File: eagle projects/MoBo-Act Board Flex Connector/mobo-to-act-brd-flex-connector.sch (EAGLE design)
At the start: 2 parts

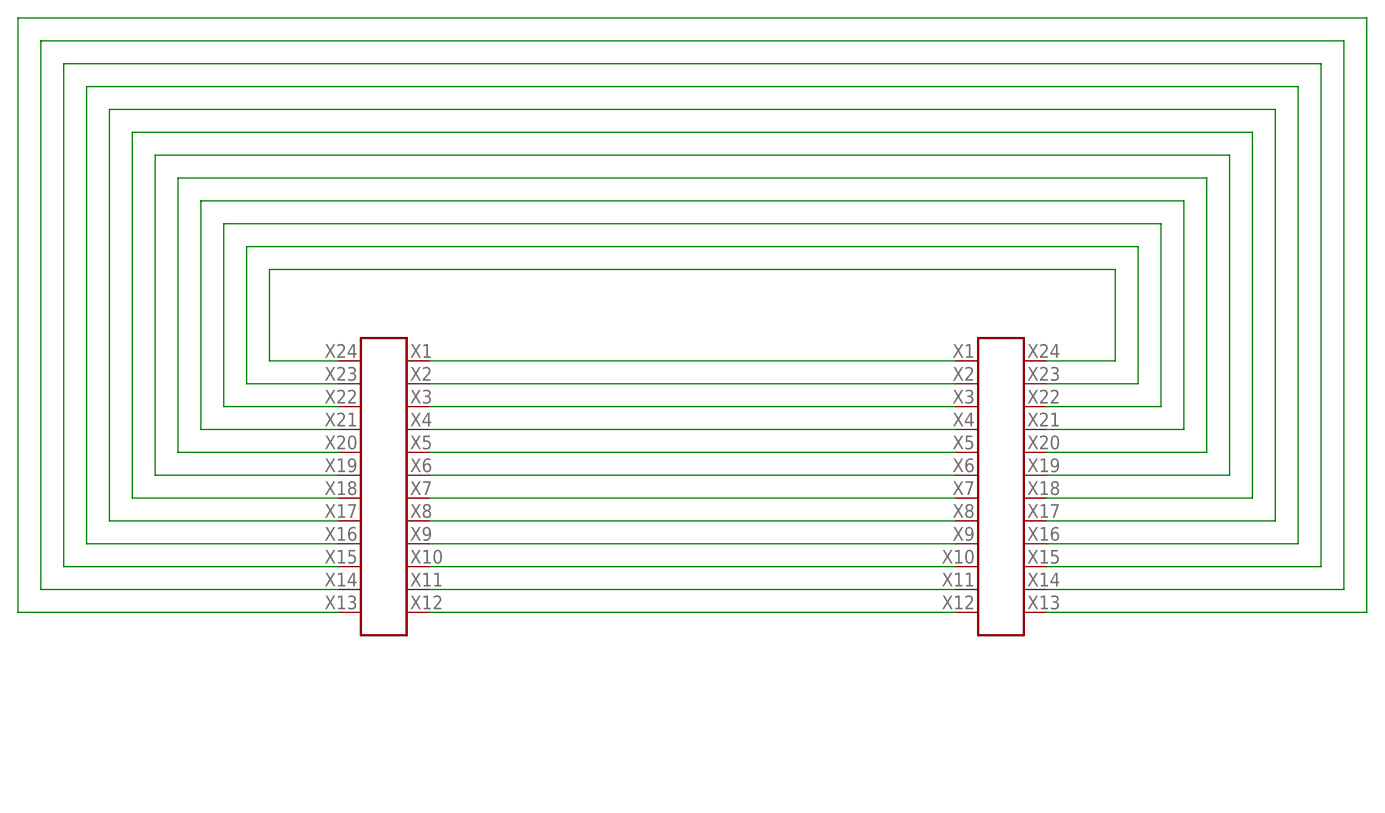
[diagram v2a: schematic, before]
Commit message: Fixed Connector Boards
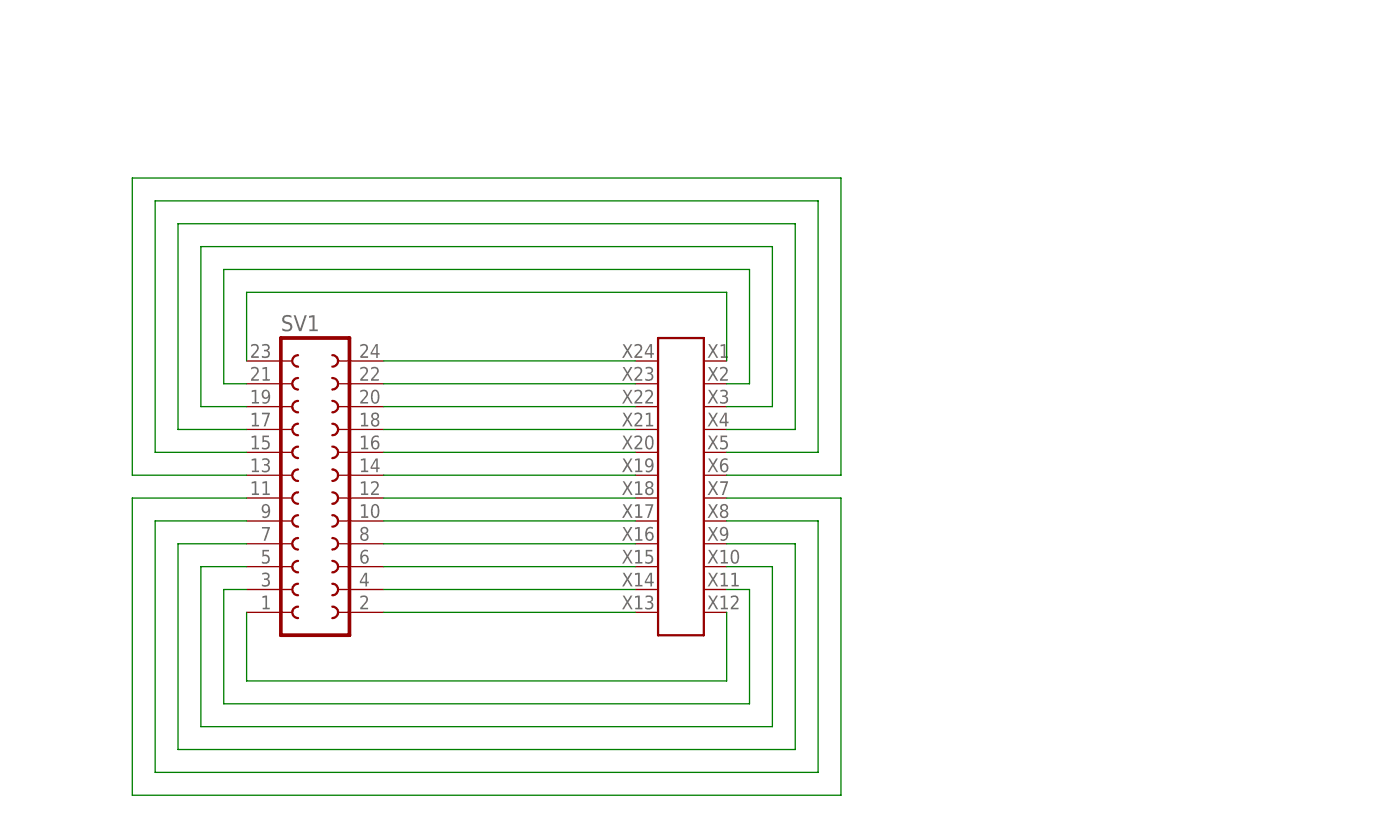
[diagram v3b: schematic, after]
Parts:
- removed U$1: 12X2_SMD_2.54MM_HEADER, SMD_headers:12X2_SMD_2.54MM_HEADER
- added SV1: (no value), con-lsta:FE12-2
- U$2: value 12X2_MIRRORED_SMD_2.54MM_HEADER -> 12X2_SMD_2.54MM_HEADER; device SMD_headers:12X2_MIRRORED_SMD_2.54MM_HEADER -> SMD_headers:12X2_SMD_2.54MM_HEADER
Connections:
- net N$1: now also SV1.1, U$2.P$12; no longer U$1.P$1, U$2.P$24
- net N$10: now also SV1.16, U$2.P$20; no longer U$1.P$10, U$2.P$15
- net N$11: now also SV1.18, U$2.P$21; no longer U$1.P$11, U$2.P$14
- net N$12: now also SV1.20, U$2.P$22; no longer U$1.P$12, U$2.P$13
- net N$13: now also SV1.22, U$2.P$23; no longer U$1.P$24, U$2.P$1
- net N$14: now also SV1.24, U$2.P$24; no longer U$1.P$23, U$2.P$2
- net N$15: now also SV1.3, U$2.P$11; no longer U$1.P$22, U$2.P$3
- net N$16: now also SV1.5, U$2.P$10; no longer U$1.P$21, U$2.P$4
- net N$17: now also SV1.21, U$2.P$2; no longer U$1.P$20, U$2.P$5
- net N$18: now also SV1.19, U$2.P$3; no longer U$1.P$19, U$2.P$6
- net N$19: now also SV1.7, U$2.P$9; no longer U$1.P$18, U$2.P$7
- net N$2: now also SV1.23, U$2.P$1; no longer U$1.P$2, U$2.P$23
- net N$20: now also SV1.17, U$2.P$4; no longer U$1.P$17, U$2.P$8
- net N$21: now also SV1.9, U$2.P$8; no longer U$1.P$16, U$2.P$9
- net N$22: now also SV1.15, U$2.P$5; no longer U$1.P$15, U$2.P$10
- net N$23: now also SV1.13, U$2.P$6; no longer U$1.P$14, U$2.P$11
- net N$24: now also SV1.11, U$2.P$7; no longer U$1.P$13, U$2.P$12
- net N$3: now also SV1.2, U$2.P$13; no longer U$1.P$3, U$2.P$22
- net N$4: now also SV1.4, U$2.P$14; no longer U$1.P$4, U$2.P$21
- net N$5: now also SV1.6, U$2.P$15; no longer U$1.P$5, U$2.P$20
- net N$6: now also SV1.8, U$2.P$16; no longer U$1.P$6, U$2.P$19
- net N$7: now also SV1.10, U$2.P$17; no longer U$1.P$7, U$2.P$18
- net N$8: now also SV1.12, U$2.P$18; no longer U$1.P$8, U$2.P$17
- net N$9: now also SV1.14, U$2.P$19; no longer U$1.P$9, U$2.P$16
